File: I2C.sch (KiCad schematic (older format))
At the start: 10 parts

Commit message: Erste fertige Version
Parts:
- added BT?: Battery_Cell, symbol Device:Battery_Cell
- added C?: 220n, symbol Device:C_Small
- added C?: 1µ, symbol Device:C_Small
- added R?: 200k, symbol Device:R_Small
- added R?: 50m, symbol Device:R_Small
- added R?: 1k, symbol Device:R_Small
- added U?: STC3100, symbol HS-Wismar:STC3100
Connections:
- net GND: now also C?.2, C?.2, R?.2, R?.2, U?.5 (GND)
- net SCL: now also U?.4 (SCL)
- net SDA: now also U?.3 (SDA)
- new net: R?.1, U?.2 (ROSC)
- new net: BT?.2 (-), R?.1, U?.6 (CG)
- new net: C?.1, R?.2, U?.8 (VIN)
- new net +BATT: BT?.1 (+), C?.1, R?.1, U?.7 (VCC)
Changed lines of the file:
@@
 $Descr A4 11693 8268
 encoding utf-8
-Sheet 9 10
+Sheet 8 10
 Title ""
 Date ""
@@
 $EndComp
 Wire Wire Line
-	2450 2250 2450 4400
-Wire Wire Line
-	2650 4300 2650 2350
+	2450 2250 2450 3450
+Wire Wire Line
+	2650 4300 2650 3550
 $Comp
 L power:GND #PWR?
@@
 Wire Wire Line
 	5450 5350 5450 5050
+$Comp
+L HS-Wismar:STC3100 U?
+U 1 1 5F025B7B
+P 6000 2600
+F 0 "U?" H 6325 3275 50  0000 C CNN
+F 1 "STC3100" H 6325 3184 50  0000 C CNN
+F 2 "" H 6000 2600 50  0001 C CNN
+F 3 "" H 6000 2600 50  0001 C CNN
+	1    6000 2600
+	1    0    0    -1
+$EndComp
+Wire Wire Line
+	5900 2300 5050 2300
+Wire Wire Line
+	5050 2300 5050 3450
+Wire Wire Line
+	5050 3450 2450 3450
+Connection ~ 2450 3450
+Wire Wire Line
+	2450 3450 2450 4400
+Wire Wire Line
+	5900 2400 5150 2400
+Wire Wire Line
+	5150 2400 5150 3550
+Wire Wire Line
+	5150 3550 2650 3550
+Connection ~ 2650 3550
+Wire Wire Line
+	2650 3550 2650 2350
+$Comp
+L Device:R_Small R?
+U 1 1 5F02B055
+P 5550 2800
+F 0 "R?" H 5609 2846 50  0000 L CNN
+F 1 "200k" H 5609 2755 50  0000 L CNN
+F 2 "" H 5550 2800 50  0001 C CNN
+F 3 "~" H 5550 2800 50  0001 C CNN
+	1    5550 2800
+	1    0    0    -1
+$EndComp
+Wire Wire Line
+	5550 2700 5550 2150
+Wire Wire Line
+	5550 2150 5900 2150
+$Comp
+L power:GND #PWR?
+U 1 1 5F02CA9E
+P 5550 3050
+F 0 "#PWR?" H 5550 2800 50  0001 C CNN
+F 1 "GND" H 5555 2877 50  0000 C CNN
+F 2 "" H 5550 3050 50  0001 C CNN
+F 3 "" H 5550 3050 50  0001 C CNN
+	1    5550 3050
+	1    0    0    -1
+$EndComp
+Wire Wire Line
+	5550 3050 5550 2900
+$Comp
+L Device:Battery_Cell BT?
+U 1 1 5F02E8A9
+P 7450 2400
+F 0 "BT?" H 7568 2450 50  0000 L CNN
+F 1 "Battery_Cell" H 7568 2405 50  0001 L CNN
+F 2 "" V 7450 2460 50  0001 C CNN
+F 3 "~" V 7450 2460 50  0001 C CNN
+	1    7450 2400
+	1    0    0    -1
+$EndComp
+$Comp
+L Device:R_Small R?
+U 1 1 5F031F1C
+P 7450 2800
+F 0 "R?" H 7509 2846 50  0000 L CNN
+F 1 "50m" H 7509 2755 50  0000 L CNN
+F 2 "" H 7450 2800 50  0001 C CNN
+F 3 "~" H 7450 2800 50  0001 C CNN
+	1    7450 2800
+	1    0    0    -1
+$EndComp
+Wire Wire Line
+	6750 2550 7450 2550
+Wire Wire Line
+	7450 2550 7450 2500
+Wire Wire Line
+	7450 2550 7450 2700
+Connection ~ 7450 2550
+$Comp
+L power:GND #PWR?
+U 1 1 5F035075
+P 7450 3050
+F 0 "#PWR?" H 7450 2800 50  0001 C CNN
+F 1 "GND" H 7455 2877 50  0000 C CNN
+F 2 "" H 7450 3050 50  0001 C CNN
+F 3 "" H 7450 3050 50  0001 C CNN
+	1    7450 3050
+	1    0    0    -1
+$EndComp
+Wire Wire Line
+	7450 3050 7450 2900
+Wire Wire Line
+	6750 2150 7000 2150
+Wire Wire Line
+	7450 2150 7450 2200
+$Comp
+L power:+BATT #PWR?
+U 1 1 5F038F3C
+P 7450 1450
+F 0 "#PWR?" H 7450 1300 50  0001 C CNN
+F 1 "+BATT" H 7465 1623 50  0000 C CNN
+F 2 "" H 7450 1450 50  0001 C CNN
+F 3 "" H 7450 1450 50  0001 C CNN
+	1    7450 1450
+	1    0    0    -1
+$EndComp
+Wire Wire Line
+	7450 1450 7450 2150
+Connection ~ 7450 2150
+$Comp
+L Device:C_Small C?
+U 1 1 5F03D903
+P 7000 2800
+F 0 "C?" H 7092 2846 50  0000 L CNN
+F 1 "220n" H 7092 2755 50  0000 L CNN
+F 2 "" H 7000 2800 50  0001 C CNN
+F 3 "~" H 7000 2800 50  0001 C CNN
+	1    7000 2800
+	1    0    0    -1
+$EndComp
+$Comp
+L Device:C_Small C?
+U 1 1 5F03E815
+P 7800 2350
+F 0 "C?" H 7892 2396 50  0000 L CNN
+F 1 "1µ" H 7892 2305 50  0000 L CNN
+F 2 "" H 7800 2350 50  0001 C CNN
+F 3 "~" H 7800 2350 50  0001 C CNN
+	1    7800 2350
+	1    0    0    -1
+$EndComp
+$Comp
+L Device:R_Small R?
+U 1 1 5F03EB5A
+P 7000 2250
+F 0 "R?" H 7059 2296 50  0000 L CNN
+F 1 "1k" H 7059 2205 50  0000 L CNN
+F 2 "" H 7000 2250 50  0001 C CNN
+F 3 "~" H 7000 2250 50  0001 C CNN
+	1    7000 2250
+	1    0    0    -1
+$EndComp
+Connection ~ 7000 2150
+Wire Wire Line
+	7000 2150 7450 2150
+Wire Wire Line
+	6750 2350 7000 2350
+Wire Wire Line
+	7000 2350 7000 2700
+Connection ~ 7000 2350
+$Comp
+L power:GND #PWR?
+U 1 1 5F041DCD
+P 7000 3050
+F 0 "#PWR?" H 7000 2800 50  0001 C CNN
+F 1 "GND" H 7005 2877 50  0000 C CNN
+F 2 "" H 7000 3050 50  0001 C CNN
+F 3 "" H 7000 3050 50  0001 C CNN
+	1    7000 3050
+	1    0    0    -1
+$EndComp
+Wire Wire Line
+	7000 3050 7000 2900
+$Comp
+L power:+BATT #PWR?
+U 1 1 5F044900
+P 7800 1450
+F 0 "#PWR?" H 7800 1300 50  0001 C CNN
+F 1 "+BATT" H 7815 1623 50  0000 C CNN
+F 2 "" H 7800 1450 50  0001 C CNN
+F 3 "" H 7800 1450 50  0001 C CNN
+	1    7800 1450
+	1    0    0    -1
+$EndComp
+Wire Wire Line
+	7800 1450 7800 2250
+$Comp
+L power:GND #PWR?
+U 1 1 5F0476E8
+P 7800 3050
+F 0 "#PWR?" H 7800 2800 50  0001 C CNN
+F 1 "GND" H 7805 2877 50  0000 C CNN
+F 2 "" H 7800 3050 50  0001 C CNN
+F 3 "" H 7800 3050 50  0001 C CNN
+	1    7800 3050
+	1    0    0    -1
+$EndComp
+Wire Wire Line
+	7800 3050 7800 2450
+$Comp
+L power:GND #PWR?
+U 1 1 5F04B71B
+P 6350 3050
+F 0 "#PWR?" H 6350 2800 50  0001 C CNN
+F 1 "GND" H 6355 2877 50  0000 C CNN
+F 2 "" H 6350 3050 50  0001 C CNN
+F 3 "" H 6350 3050 50  0001 C CNN
+	1    6350 3050
+	1    0    0    -1
+$EndComp
+Wire Wire Line
+	6350 3050 6350 2700
 $EndSCHEMATC

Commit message: Externe Spannungsversorgung
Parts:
- BT?: value Battery_Cell -> 18650_Cell
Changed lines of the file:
@@
 P 7450 2400
 F 0 "BT?" H 7568 2450 50  0000 L CNN
-F 1 "Battery_Cell" H 7568 2405 50  0001 L CNN
+F 1 "18650_Cell" H 7568 2405 50  0001 L CNN
 F 2 "" V 7450 2460 50  0001 C CNN
 F 3 "~" V 7450 2460 50  0001 C CNN

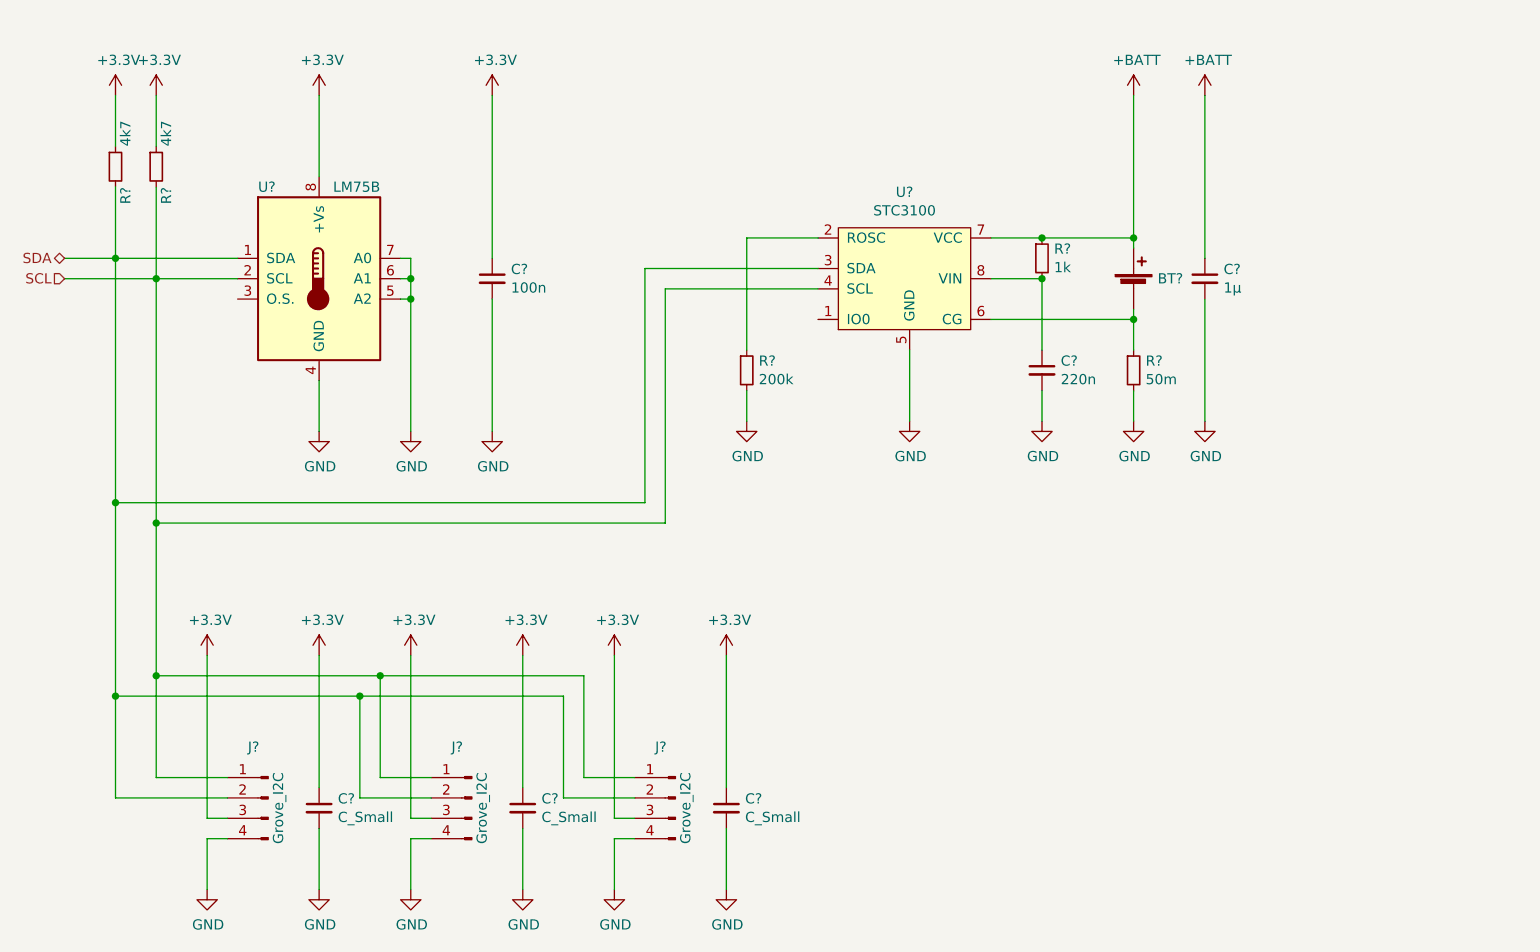
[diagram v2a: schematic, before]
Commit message: Bauteile grob platziert
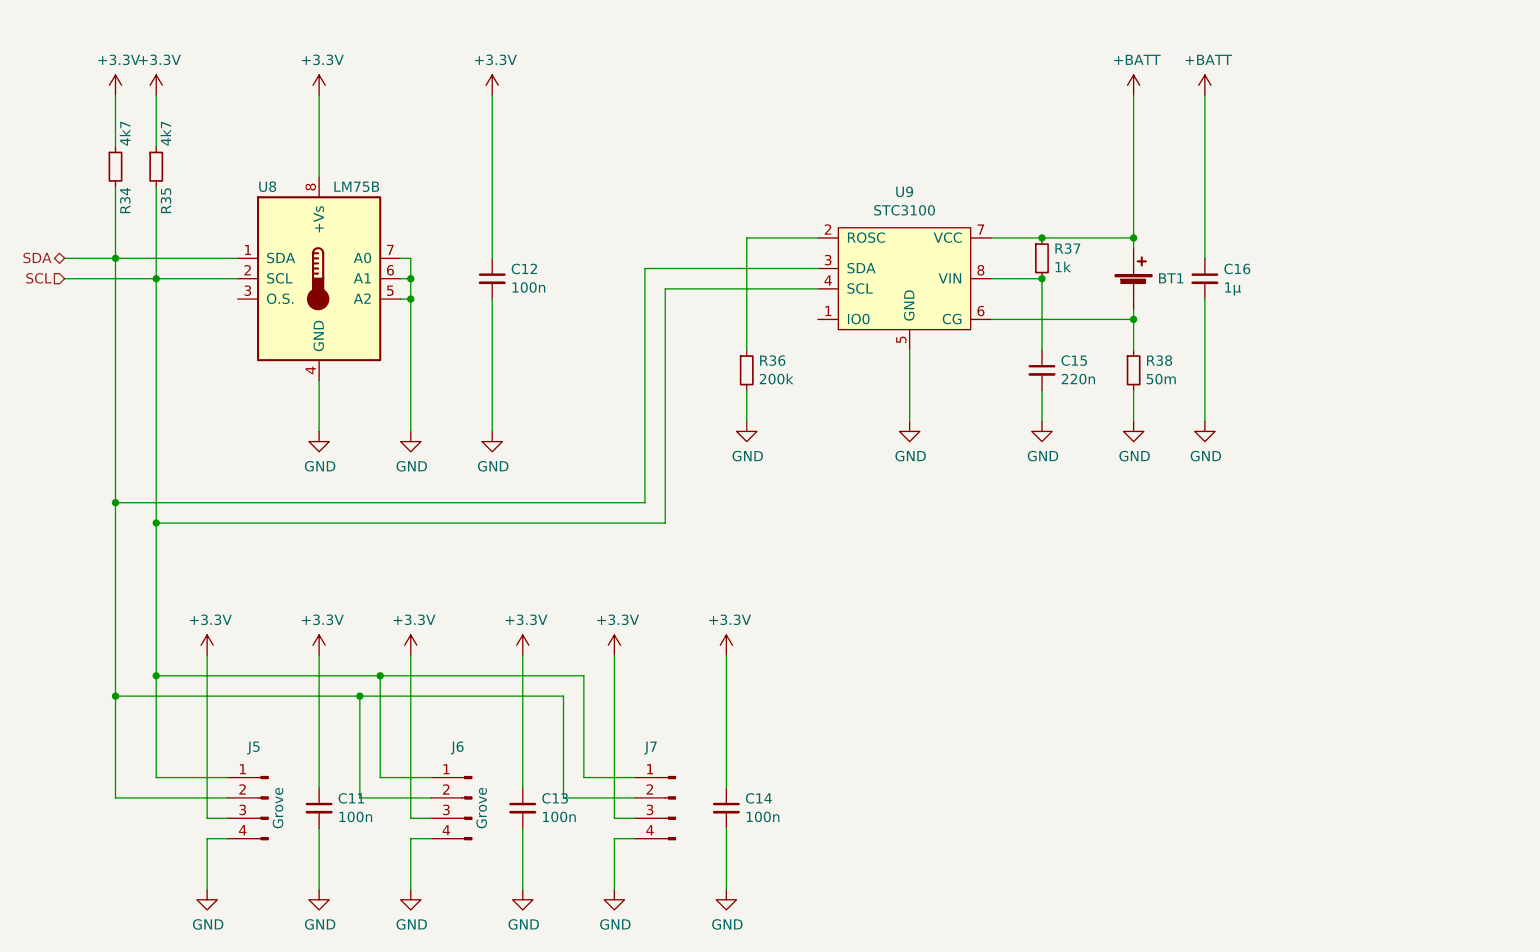
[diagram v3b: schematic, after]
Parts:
- removed J?: Grove_I2C, symbol Connector:Conn_01x04_Male
- added J7: Conn_01x04_Male, Connector_PinHeader_2.54mm:PinHeader_1x04_P2.54mm_Vertical, symbol Connector:Conn_01x04_Male
- BT1: renamed from BT?; footprint (none) -> Battery:BatteryHolder_Keystone_1042_1x18650
- C11, C13, C14: renamed from C?; value C_Small -> 100n; footprint (none) -> Capacitor_SMD:C_0603_1608Metric_Pad1.05x0.95mm_HandSolder
- C12, C15, C16: renamed from C?; footprint (none) -> Capacitor_SMD:C_0603_1608Metric_Pad1.05x0.95mm_HandSolder
- J5, J6: renamed from J?; value Grove_I2C -> Grove; footprint (none) -> Connector:NS-Tech_Grove_1x04_P2mm_Vertical
- R34, R35, R36, R37: renamed from R?; footprint (none) -> Resistor_SMD:R_0603_1608Metric_Pad1.05x0.95mm_HandSolder
- R38: renamed from R?; footprint (none) -> Resistor_SMD:R_1206_3216Metric_Pad1.42x1.75mm_HandSolder
- U8: renamed from U?; footprint (none) -> Package_SO:SO-8_3.9x4.9mm_P1.27mm
- U9: renamed from U?; footprint (none) -> Package_SO:MSOP-8_3x3mm_P0.65mm
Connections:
- net +3V3: now also J7.3 (Pin_3)
- net GND: now also J7.4 (Pin_4)
- net SCL: now also J7.1 (Pin_1)
- net SDA: now also J7.2 (Pin_2)

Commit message: Alle Bauteile platziert
Alle Bauteile sind grob plaziert.
Einige Bauteile sollten noch umplaziert werden (u. a. die Jumper links neben Groov-Con, RGB-LED,).
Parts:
- BT1: symbol Device:Battery_Cell -> MCT_Labor_5529-rescue:Battery_Cell-Device
- C11, C12, C13, C14, C15, C16: symbol Device:C_Small -> MCT_Labor_5529-rescue:C_Small-Device
- J5, J6, J7: symbol Connector:Conn_01x04_Male -> MCT_Labor_5529-rescue:Conn_01x04_Male-Connector
- R34, R35, R36, R37, R38: symbol Device:R_Small -> MCT_Labor_5529-rescue:R_Small-Device
- U8: symbol Sensor_Temperature:LM75B -> MCT_Labor_5529-rescue:LM75B-Sensor_Temperature
- U9: symbol HS-Wismar:STC3100 -> MCT_Labor_5529-rescue:STC3100-HS-Wismar
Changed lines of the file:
@@
 $EndDescr
 $Comp
-L Sensor_Temperature:LM75B U8
+L MCT_Labor_5529-rescue:LM75B-Sensor_Temperature U8
 U 1 1 5EFEA302
 P 3450 2350
@@
 	2200 2350 2650 2350
 $Comp
-L Device:R_Small R34
+L MCT_Labor_5529-rescue:R_Small-Device R34
 U 1 1 5EFEB920
 P 2450 1800
@@
 $EndComp
 $Comp
-L Device:R_Small R35
+L MCT_Labor_5529-rescue:R_Small-Device R35
 U 1 1 5EFEBB93
 P 2650 1800
@@
 	2650 2350 3050 2350
 $Comp
-L power:+3.3V #PWR0165
+L MCT_Labor_5529-rescue:+3.3V-power #PWR0165
 U 1 1 5EFEBF5B
 P 3450 1450
@@
 $EndComp
 $Comp
-L power:+3.3V #PWR0166
+L MCT_Labor_5529-rescue:+3.3V-power #PWR0166
 U 1 1 5EFEC196
 P 2450 1450
@@
 $EndComp
 $Comp
-L power:+3.3V #PWR0167
+L MCT_Labor_5529-rescue:+3.3V-power #PWR0167
 U 1 1 5EFEC31B
 P 2650 1450
@@
 	3450 1450 3450 1850
 $Comp
-L power:GND #PWR0168
+L MCT_Labor_5529-rescue:GND-power #PWR0168
 U 1 1 5EFEDDCF
 P 3450 3100
@@
 	3450 3100 3450 2850
 $Comp
-L Device:C_Small C12
+L MCT_Labor_5529-rescue:C_Small-Device C12
 U 1 1 5EFEE13D
 P 4300 2350
@@
 $EndComp
 $Comp
-L power:+3.3V #PWR0169
+L MCT_Labor_5529-rescue:+3.3V-power #PWR0169
 U 1 1 5EFEE61F
 P 4300 1450
@@
 $EndComp
 $Comp
-L power:GND #PWR0170
+L MCT_Labor_5529-rescue:GND-power #PWR0170
 U 1 1 5EFEE818
 P 4300 3100
@@
 	4300 2250 4300 1450
 $Comp
-L power:GND #PWR0171
+L MCT_Labor_5529-rescue:GND-power #PWR0171
 U 1 1 5EFEEF44
 P 3900 3100
@@
 	3900 2450 3900 2350
 $Comp
-L Connector:Conn_01x04_Male J5
+L MCT_Labor_5529-rescue:Conn_01x04_Male-Connector J5
 U 1 1 5EFF0AF9
 P 3200 4900
@@
 	2650 4300 2650 3550
 $Comp
-L power:GND #PWR0172
+L MCT_Labor_5529-rescue:GND-power #PWR0172
 U 1 1 5EFF326D
 P 2900 5350
@@
 $EndComp
 $Comp
-L power:+3.3V #PWR0173
+L MCT_Labor_5529-rescue:+3.3V-power #PWR0173
 U 1 1 5EFF35F9
 P 2900 4200
@@
 	2900 5100 2900 5350
 $Comp
-L Connector:Conn_01x04_Male J6
+L MCT_Labor_5529-rescue:Conn_01x04_Male-Connector J6
 U 1 1 5EFFA8F1
 P 4200 4900
@@
 $EndComp
 $Comp
-L power:GND #PWR0174
+L MCT_Labor_5529-rescue:GND-power #PWR0174
 U 1 1 5EFFA8F7
 P 3900 5350
@@
 $EndComp
 $Comp
-L power:+3.3V #PWR0175
+L MCT_Labor_5529-rescue:+3.3V-power #PWR0175
 U 1 1 5EFFA8FD
 P 3900 4200
@@
 	3900 5100 3900 5350
 $Comp
-L power:GND #PWR0176
+L MCT_Labor_5529-rescue:GND-power #PWR0176
 U 1 1 5EFFBA11
 P 4900 5350
@@
 $EndComp
 $Comp
-L power:+3.3V #PWR0177
+L MCT_Labor_5529-rescue:+3.3V-power #PWR0177
 U 1 1 5EFFBA17
 P 4900 4200
@@
 Connection ~ 3750 4300
 $Comp
-L Device:C_Small C11
+L MCT_Labor_5529-rescue:C_Small-Device C11
 U 1 1 5F0051F8
 P 3450 4950
@@
 $EndComp
 $Comp
-L power:GND #PWR0178
+L MCT_Labor_5529-rescue:GND-power #PWR0178
 U 1 1 5F00549D
 P 3450 5350
@@
 $EndComp
 $Comp
-L power:+3.3V #PWR0179
+L MCT_Labor_5529-rescue:+3.3V-power #PWR0179
 U 1 1 5F0057BE
 P 3450 4200
@@
 	3450 5350 3450 5050
 $Comp
-L Device:C_Small C13
+L MCT_Labor_5529-rescue:C_Small-Device C13
 U 1 1 5F008876
 P 4450 4950
@@
 $EndComp
 $Comp
-L power:GND #PWR0180
+L MCT_Labor_5529-rescue:GND-power #PWR0180
 U 1 1 5F00887C
 P 4450 5350
@@
 $EndComp
 $Comp
-L power:+3.3V #PWR0181
+L MCT_Labor_5529-rescue:+3.3V-power #PWR0181
 U 1 1 5F008882
 P 4450 4200
@@
 	4450 5350 4450 5050
 $Comp
-L Device:C_Small C14
+L MCT_Labor_5529-rescue:C_Small-Device C14
 U 1 1 5F00961C
 P 5450 4950
@@
 $EndComp
 $Comp
-L power:GND #PWR0182
+L MCT_Labor_5529-rescue:GND-power #PWR0182
 U 1 1 5F009622
 P 5450 5350
@@
 $EndComp
 $Comp
-L power:+3.3V #PWR0183
+L MCT_Labor_5529-rescue:+3.3V-power #PWR0183
 U 1 1 5F009628
 P 5450 4200
@@
 	5450 5350 5450 5050
 $Comp
-L HS-Wismar:STC3100 U9
+L MCT_Labor_5529-rescue:STC3100-HS-Wismar U9
 U 1 1 5F025B7B
 P 6000 2600
@@
 	2650 3550 2650 2350
 $Comp
-L Device:R_Small R36
+L MCT_Labor_5529-rescue:R_Small-Device R36
 U 1 1 5F02B055
 P 5550 2800
@@
 	5550 2150 5900 2150
 $Comp
-L power:GND #PWR0184
+L MCT_Labor_5529-rescue:GND-power #PWR0184
 U 1 1 5F02CA9E
 P 5550 3050
@@
 	5550 3050 5550 2900
 $Comp
-L Device:Battery_Cell BT1
+L MCT_Labor_5529-rescue:Battery_Cell-Device BT1
 U 1 1 5F02E8A9
 P 7450 2400
@@
 $EndComp
 $Comp
-L Device:R_Small R38
+L MCT_Labor_5529-rescue:R_Small-Device R38
 U 1 1 5F031F1C
 P 7450 2800
@@
 Connection ~ 7450 2550
 $Comp
-L power:GND #PWR0185
+L MCT_Labor_5529-rescue:GND-power #PWR0185
 U 1 1 5F035075
 P 7450 3050
@@
 	7450 2150 7450 2200
 $Comp
-L power:+BATT #PWR0186
+L MCT_Labor_5529-rescue:+BATT-power #PWR0186
 U 1 1 5F038F3C
 P 7450 1450
@@
 Connection ~ 7450 2150
 $Comp
-L Device:C_Small C15
+L MCT_Labor_5529-rescue:C_Small-Device C15
 U 1 1 5F03D903
 P 7000 2800
@@
 $EndComp
 $Comp
-L Device:C_Small C16
+L MCT_Labor_5529-rescue:C_Small-Device C16
 U 1 1 5F03E815
 P 7800 2350
@@
 $EndComp
 $Comp
-L Device:R_Small R37
+L MCT_Labor_5529-rescue:R_Small-Device R37
 U 1 1 5F03EB5A
 P 7000 2250
@@
 Connection ~ 7000 2350
 $Comp
-L power:GND #PWR0187
+L MCT_Labor_5529-rescue:GND-power #PWR0187
 U 1 1 5F041DCD
 P 7000 3050
@@
 	7000 3050 7000 2900
 $Comp
-L power:+BATT #PWR0188
+L MCT_Labor_5529-rescue:+BATT-power #PWR0188
 U 1 1 5F044900
 P 7800 1450
@@
 	7800 1450 7800 2250
 $Comp
-L power:GND #PWR0189
+L MCT_Labor_5529-rescue:GND-power #PWR0189
 U 1 1 5F0476E8
 P 7800 3050
@@
 	7800 3050 7800 2450
 $Comp
-L power:GND #PWR0190
+L MCT_Labor_5529-rescue:GND-power #PWR0190
 U 1 1 5F04B71B
 P 6350 3050
@@
 	6350 3050 6350 2700
 $Comp
-L Connector:Conn_01x04_Male J7
+L MCT_Labor_5529-rescue:Conn_01x04_Male-Connector J7
 U 1 1 5F06F105
 P 5200 4900
